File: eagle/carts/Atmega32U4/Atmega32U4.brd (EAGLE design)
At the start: 50.2 x 61 mm, 30 parts, among them J6 USB4110-GF-A_REVB, U1 3.3V, U3 32U4, X3 16MHz

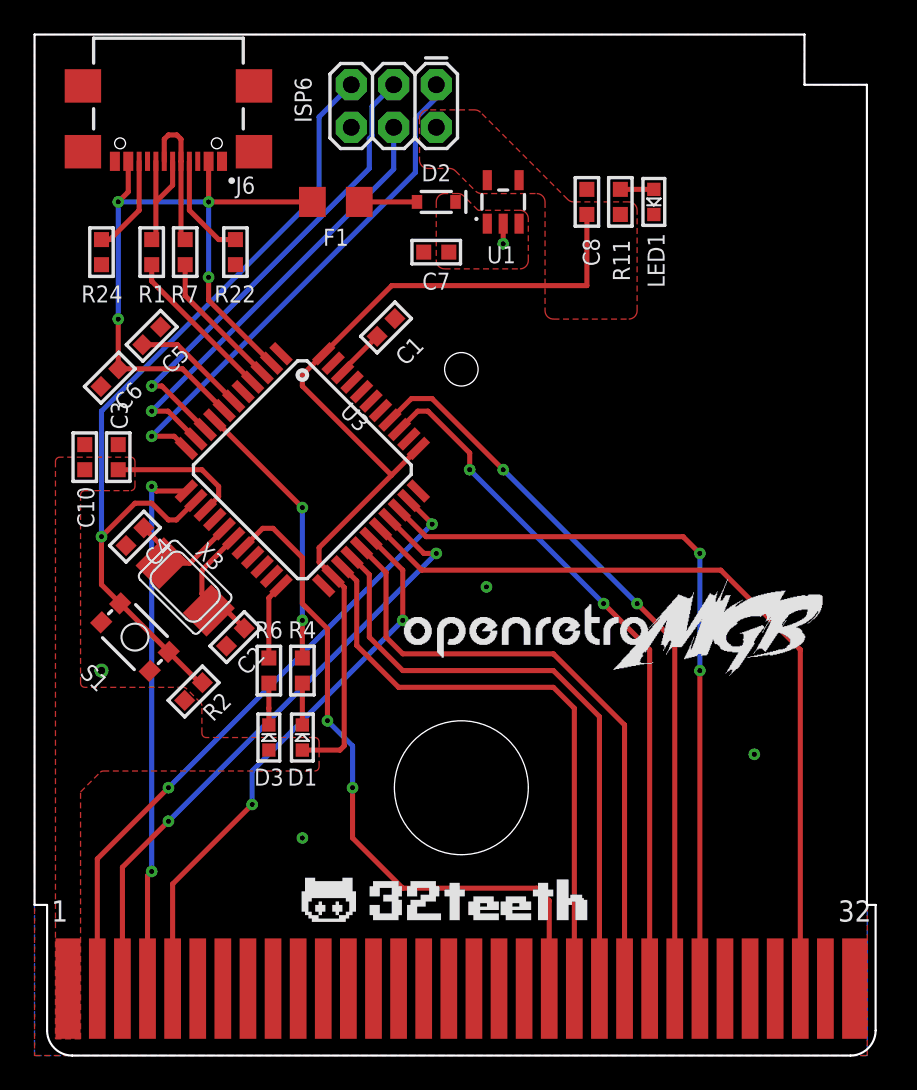
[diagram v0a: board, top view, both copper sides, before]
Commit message: feat: update Atmega32u4
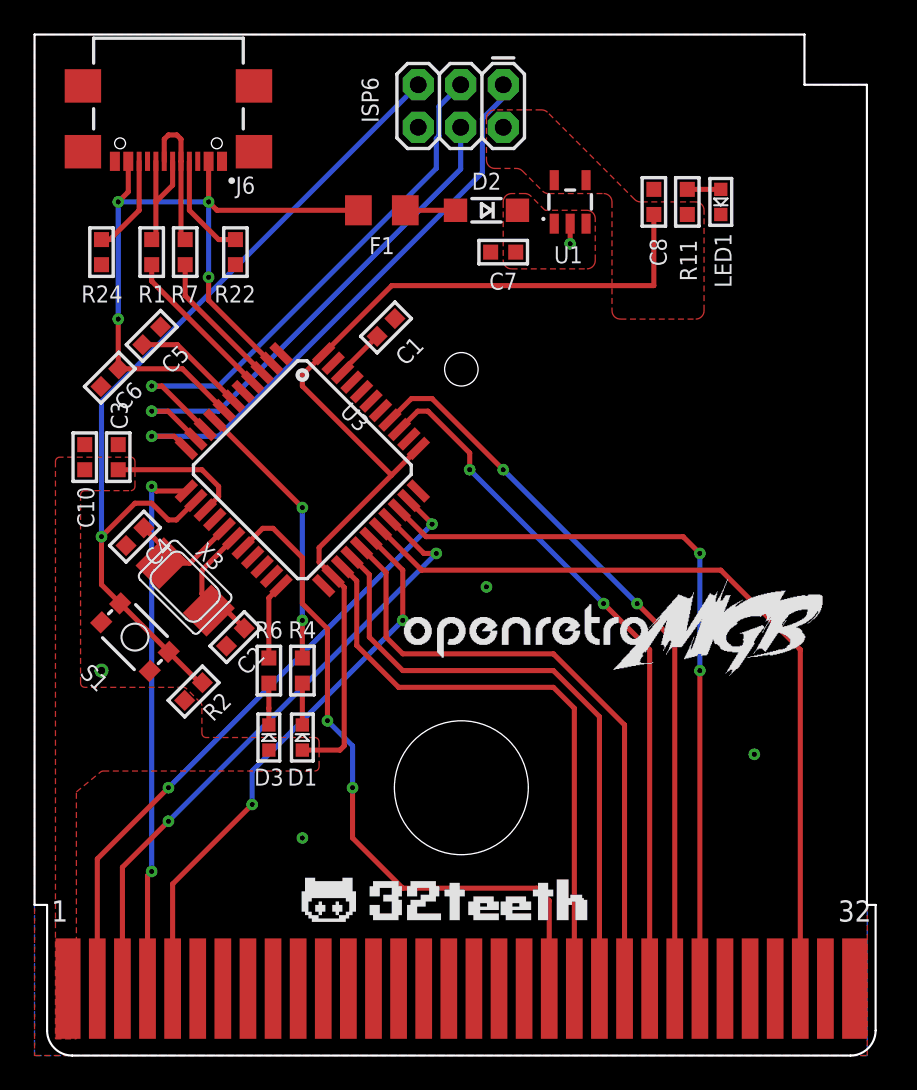
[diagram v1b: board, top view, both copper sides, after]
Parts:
- D2: device SparkFun-DiscreteSemi:SOD-323 -> RetroESP32:SOD-123
- moved C7 4.00 mm to (28.0, 48.0)
- moved C8 4.00 mm to (37.0, 51.0)
- moved ISP6 4.00 mm to (28.0, 58.0)
- moved LED1 4.00 mm to (41.0, 51.0)
- moved R11 4.00 mm to (39.0, 51.0)
- moved U1 4.00 mm to (32.0, 51.0)
- moved D2 3.04 mm to (27.0, 50.5)
- moved F1 2.80 mm to (20.8, 50.5)
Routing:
- net 3V3: track 63.3 -> 67.3 mm
- net AVR_SCK: track 28.3 -> 32.3 mm
- net AVR_MOSI: track 26.3 -> 30.3 mm
- net AVR_MISO: track 30.4 -> 34.4 mm
- net V_USB: track 45.2 -> 48.2 mm
- net AVR_RST: track 51.9 -> 53.5 mm
